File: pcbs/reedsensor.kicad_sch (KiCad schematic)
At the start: 4 parts, among them J9 Conn_01x03_Pin, SW1 SW_Reed

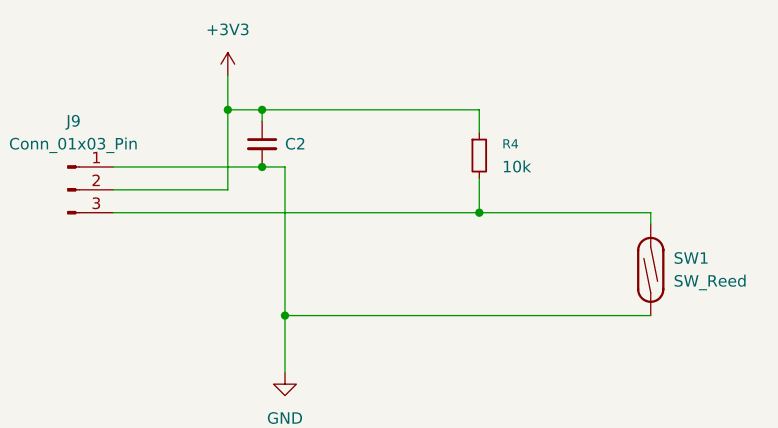
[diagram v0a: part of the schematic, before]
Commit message: add ld2450, recreate simple hall effect sensor, add ssd1306 display
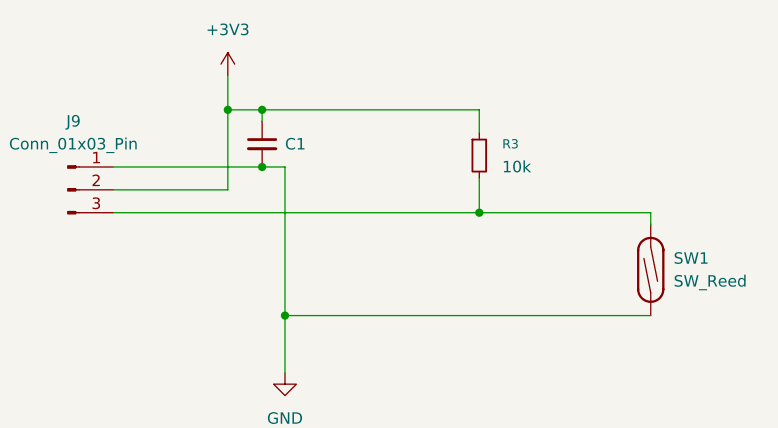
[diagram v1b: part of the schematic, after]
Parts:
- removed C2: (no value), symbol Device:C_Small
- removed R4: 10k, symbol Device:R_Small
- added C1: (no value), symbol Device:C_Small
- added R3: 10k, symbol Device:R_Small
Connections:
- net +3V3: now also C1.1, R3.1
- net GND: now also C1.2
- net at J9.3 (Pin_3), SW1.2: now also R3.2

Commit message: try to fix kicad weirdness
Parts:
- renumbered C1 to C2, R3 to R4
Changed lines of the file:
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@@
 		(dnp no)
 		(fields_autoplaced yes)
-		(property "Reference" "#PWR018"
+		(property "Reference" "#PWR019"
 			(at 91.44 88.9 0)
 			(hide yes)
@@
 			(project "monstera"
 				(path "/ed19bf13-7d2f-42f1-bf06-d29e3baf4707"
-					(reference "#PWR018")
+					(reference "#PWR019")
 					(unit 1)
 				)
@@
 		(dnp no)
 		(fields_autoplaced yes)
-		(property "Reference" "R3"
+		(property "Reference" "R4"
 			(at 115.57 57.1499 0)
 			(show_name no)
@@
 			(project "monstera"
 				(path "/ed19bf13-7d2f-42f1-bf06-d29e3baf4707"
-					(reference "R3")
+					(reference "R4")
 					(unit 1)
 				)
@@
 		(dnp no)
 		(fields_autoplaced yes)
-		(property "Reference" "#PWR016"
+		(property "Reference" "#PWR018"
 			(at 85.09 53.34 0)
 			(hide yes)
@@
 			(project "monstera"
 				(path "/ed19bf13-7d2f-42f1-bf06-d29e3baf4707"
-					(reference "#PWR016")
+					(reference "#PWR018")
 					(unit 1)
 				)
@@
 		(dnp no)
 		(fields_autoplaced yes)
-		(property "Reference" "C1"
+		(property "Reference" "C2"
 			(at 91.44 57.1562 0)
 			(show_name no)
@@
 			(project "monstera"
 				(path "/ed19bf13-7d2f-42f1-bf06-d29e3baf4707"
-					(reference "C1")
-					(unit 1)
-				)
+					(reference "C2")
+					(unit 1)
+				)

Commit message: make sensor pcbs
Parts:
- added H1, H2, H3, H4: MountingHole, MountingHole:MountingHole_2.2mm_M2, symbol Mechanical:MountingHole
- C2: footprint (none) -> Capacitor_SMD:C_0805_2012Metric_Pad1.18x1.45mm_HandSolder
- J9: footprint (none) -> Connector_JST:JST_PH_S3B-PH-K_1x03_P2.00mm_Horizontal
- R4: footprint (none) -> Resistor_SMD:R_0805_2012Metric_Pad1.20x1.40mm_HandSolder
- SW1: footprint (none) -> Button_Switch_SMD:SW_SPST_REED_CT05-XXXX-J1
